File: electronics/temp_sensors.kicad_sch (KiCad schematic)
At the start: 4 parts, among them J17 Conn_01x03, J18 Conn_01x03, J19 Conn_01x03

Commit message: no tracks, but placement looks good
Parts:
- J19: now not fitted
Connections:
- net +3V3: no longer R21.1
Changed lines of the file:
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@@
 	(wire
 		(pts
-			(xy 57.15 60.96) (xy 59.69 60.96)
+			(xy 55.88 60.96) (xy 59.69 60.96)
 		)
 		(stroke
@@
 		(exclude_from_sim no)
 		(in_bom yes)
-		(on_board yes)
-		(dnp no)
+		(on_board no)
+		(dnp yes)
 		(fields_autoplaced yes)
 		(property "Reference" "J19"
@@
 	)
 	(symbol
+		(lib_name "+3V3_1")
 		(lib_id "power:+3V3")
-		(at 57.15 60.96 0)
+		(at 55.88 60.96 0)
 		(unit 1)
 		(exclude_from_sim no)
@@
 		(fields_autoplaced yes)
 		(property "Reference" "#PWR035"
-			(at 57.15 64.77 0)
+			(at 55.88 64.77 0)
 			(effects
 				(font
@@
 		)
 		(property "Value" "+3V3"
-			(at 57.15 55.88 0)
+			(at 55.88 55.88 0)
 			(effects
 				(font
@@
 		)
 		(property "Footprint" ""
-			(at 57.15 60.96 0)
+			(at 55.88 60.96 0)
 			(effects
 				(font
@@
 		)
 		(property "Datasheet" ""
-			(at 57.15 60.96 0)
+			(at 55.88 60.96 0)
 			(effects
 				(font
@@
 		)
 		(property "Description" "Power symbol creates a global label with name \"+3V3\""
-			(at 57.15 60.96 0)
-			(effects
-				(font
+			(at 55.88 60.96 0)
+			(effects
+				(font

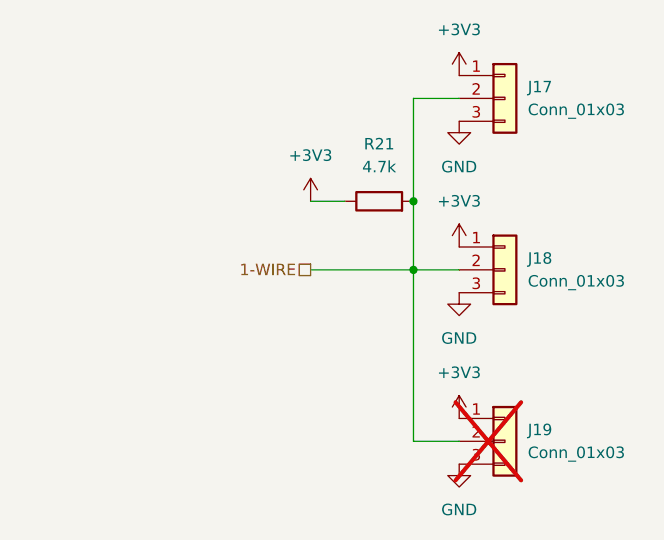
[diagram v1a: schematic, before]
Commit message: capacitors added. universal dc/dc converters
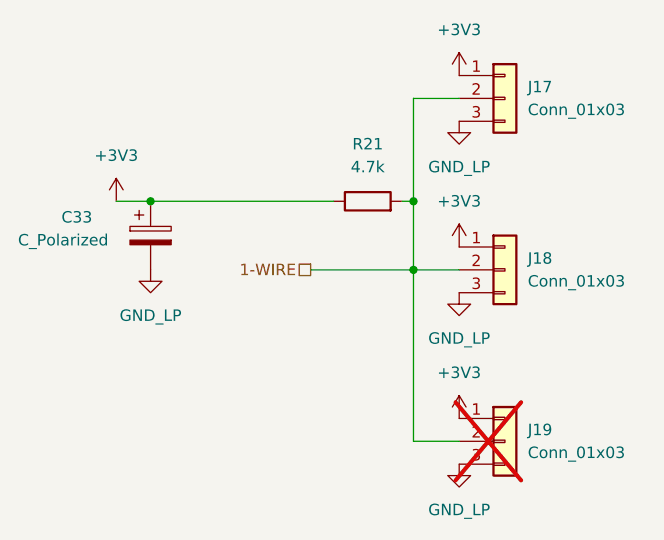
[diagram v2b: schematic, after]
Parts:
- added C33: C_Polarized, Capacitor_THT:CP_Radial_D5.0mm_P2.50mm, symbol Device:C_Polarized
- R21: footprint Resistor_SMD:R_0805_2012Metric_Pad1.20x1.40mm_HandSolder -> Resistor_SMD:R_0805_2012Metric
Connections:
- net at R21.1: now also C33.1
- net GND renamed GND_LP
- net GND_LP: now also C33.2
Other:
- moved on the sheet: R21
